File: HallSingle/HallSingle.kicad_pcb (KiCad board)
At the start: 2 copper layers, 12 x 23.5 mm, 11 parts, among them J1 Conn_01x03, U1 SS49E, U2 TS331ILT

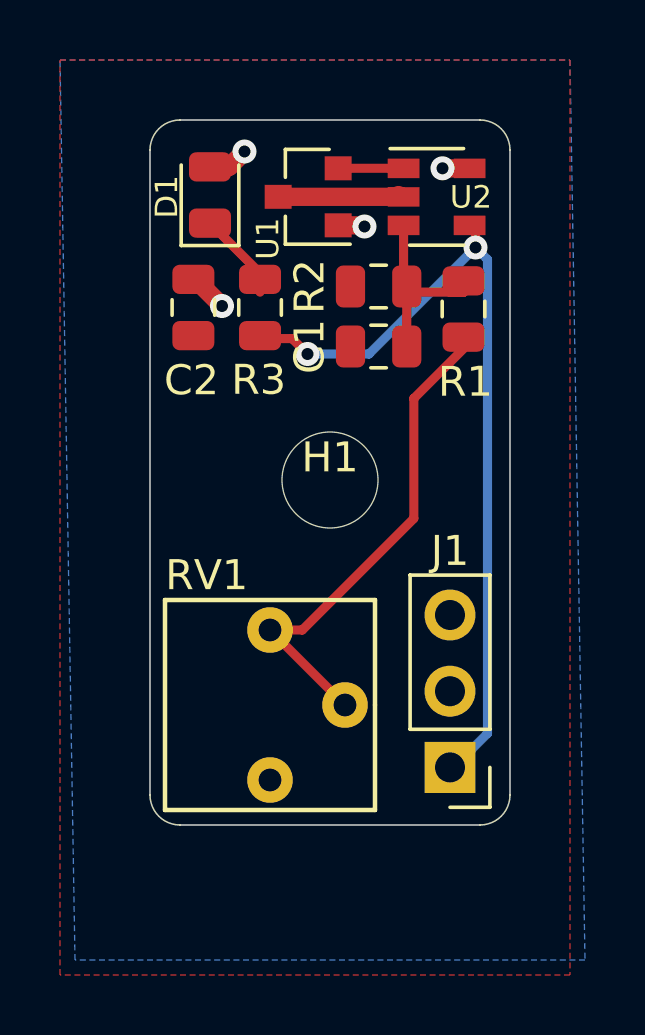
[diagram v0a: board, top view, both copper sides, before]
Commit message: added ibom and other small fixes
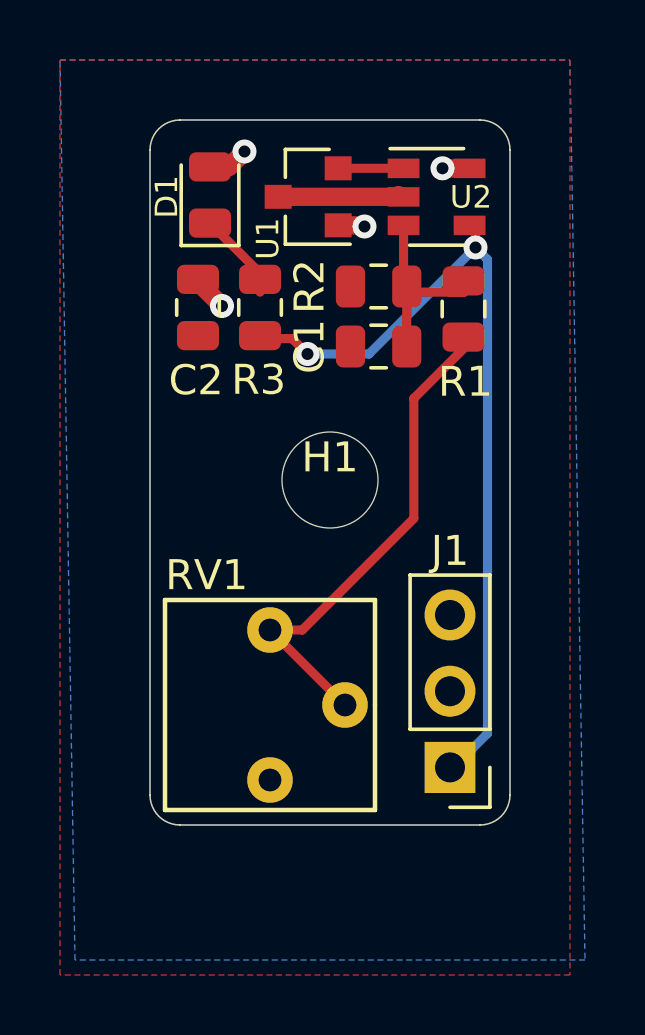
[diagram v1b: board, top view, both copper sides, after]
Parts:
- moved C2 0.15 mm to (139.6, 63.2)
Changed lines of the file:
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@@
   )
   (module HallEffect:C_0805_2012Metric (layer F.Cu)
-    (at 139.446 63.25 270)
+    (at 139.6 63.25 270)
     (descr "Capacitor SMD 0805 (2012 Metric), square (rectangular) end terminal, IPC_7351 nominal, (Body size source: https://docs.google.com/spreadsheets/d/1BsfQQcO9C6DZCsRaXUlFlo91Tg2WpOkGARC1WS5S8t0/edit?usp=sharing), generated with kicad-footprint-generator")
     (tags capacitor)
